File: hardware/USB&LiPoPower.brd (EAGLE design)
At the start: 47 x 40.5 mm, 68 parts, among them IC1 4066D, IC2 4066D, IC3 HT7750A_SOT23-3, IC4 I-02247_NJM2845, T1 IRLML5203, T2 IRLML5203, T3 IRLML5203, T4 IRLML5203

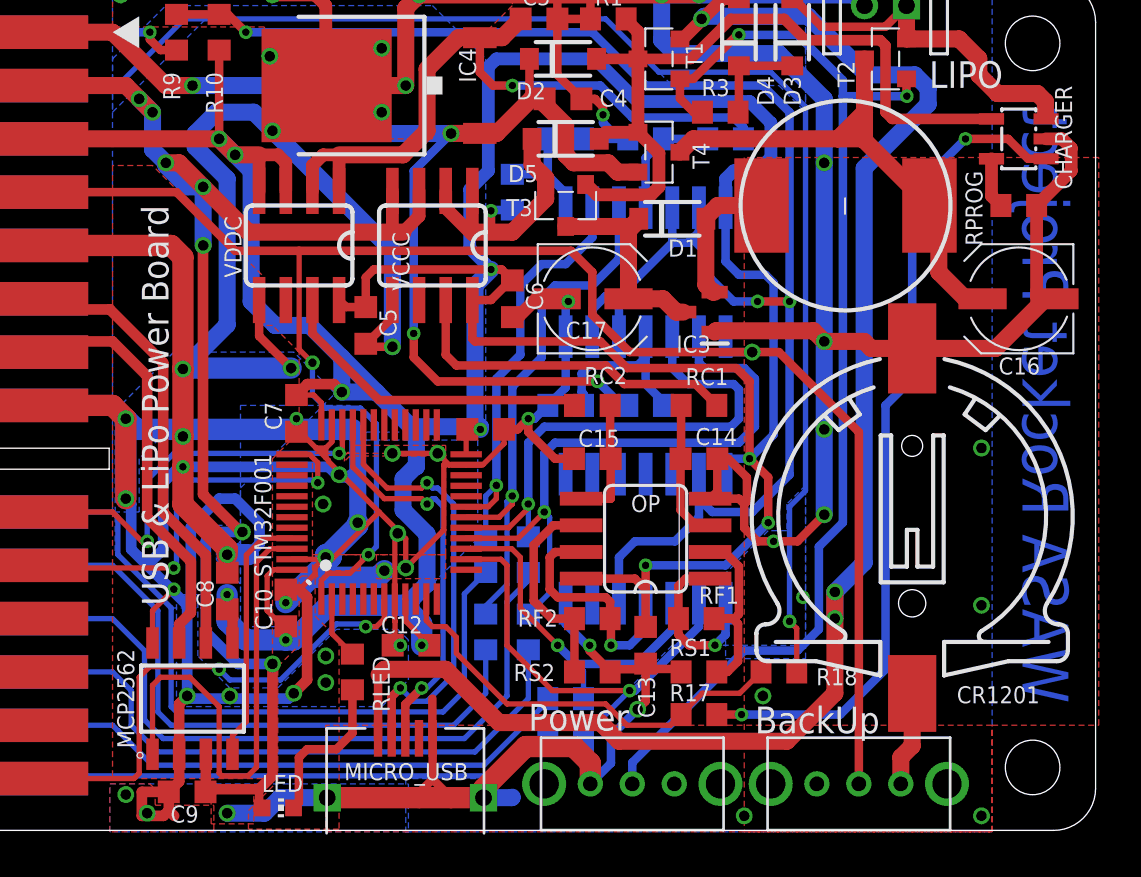
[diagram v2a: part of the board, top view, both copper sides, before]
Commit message: Clean silk print
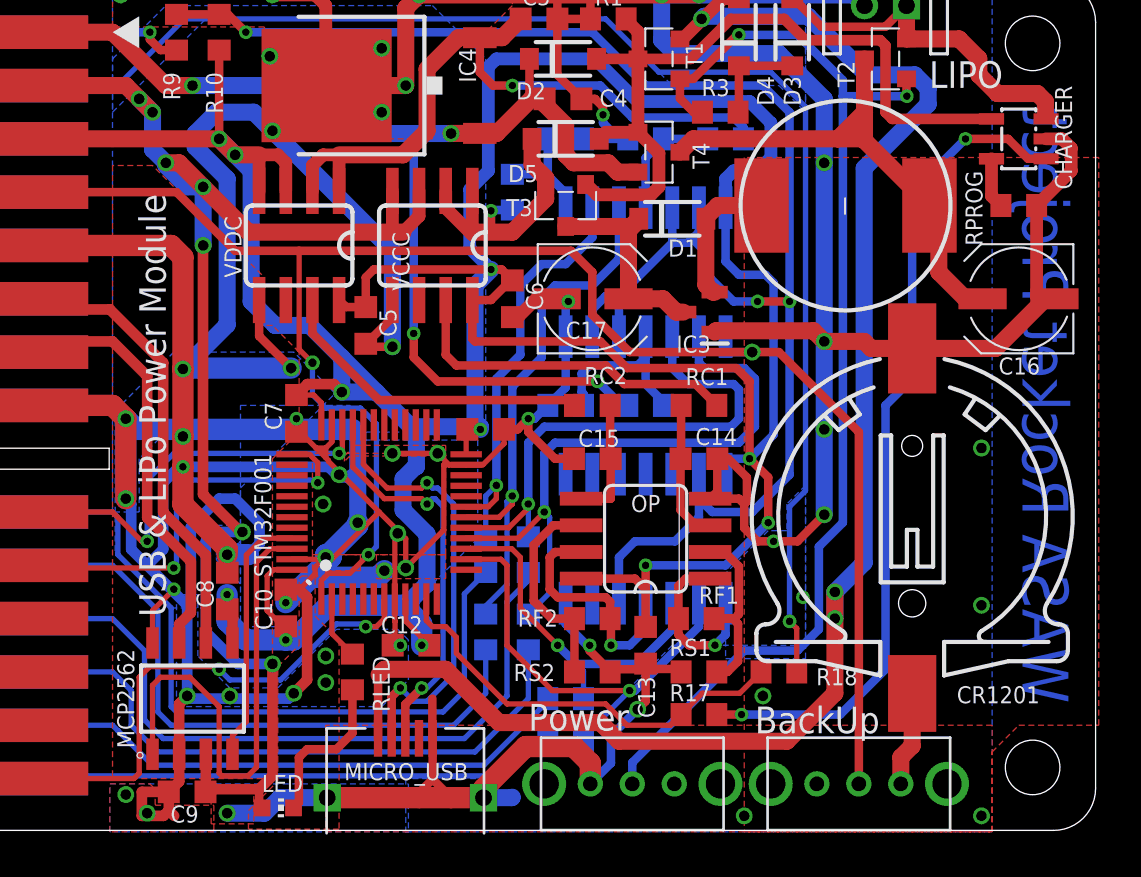
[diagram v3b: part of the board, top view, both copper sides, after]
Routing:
- net VPP: track 59.8 -> 60.7 mm
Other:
- board text added: "Designed by @fujiy0, 2019"
- board text added: "USB & LiPo Power Module"
- board text removed: "USB & LiPo Power Board"
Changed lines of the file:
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@@
 <layer number="14" name="Route14" color="22" fill="1" visible="no" active="no"/>
 <layer number="15" name="Route15" color="23" fill="1" visible="no" active="no"/>
-<layer number="16" name="Bottom" color="1" fill="1" visible="no" active="yes"/>
+<layer number="16" name="Bottom" color="1" fill="1" visible="yes" active="yes"/>
 <layer number="17" name="Pads" color="2" fill="1" visible="yes" active="yes"/>
 <layer number="18" name="Vias" color="2" fill="1" visible="yes" active="yes"/>
@@
 <layer number="20" name="Dimension" color="24" fill="1" visible="yes" active="yes"/>
 <layer number="21" name="tPlace" color="7" fill="1" visible="yes" active="yes"/>
-<layer number="22" name="bPlace" color="7" fill="1" visible="no" active="yes"/>
+<layer number="22" name="bPlace" color="7" fill="1" visible="yes" active="yes"/>
 <layer number="23" name="tOrigins" color="15" fill="1" visible="yes" active="yes"/>
-<layer number="24" name="bOrigins" color="15" fill="1" visible="no" active="yes"/>
+<layer number="24" name="bOrigins" color="15" fill="1" visible="yes" active="yes"/>
 <layer number="25" name="tNames" color="7" fill="1" visible="yes" active="yes"/>
-<layer number="26" name="bNames" color="7" fill="1" visible="no" active="yes"/>
+<layer number="26" name="bNames" color="7" fill="1" visible="yes" active="yes"/>
 <layer number="27" name="tValues" color="7" fill="1" visible="no" active="yes"/>
 <layer number="28" name="bValues" color="7" fill="1" visible="no" active="yes"/>
@@
 <layer number="38" name="bTest" color="7" fill="1" visible="no" active="yes"/>
 <layer number="39" name="tKeepout" color="4" fill="11" visible="yes" active="yes"/>
-<layer number="40" name="bKeepout" color="1" fill="11" visible="no" active="yes"/>
+<layer number="40" name="bKeepout" color="1" fill="11" visible="yes" active="yes"/>
 <layer number="41" name="tRestrict" color="4" fill="10" visible="yes" active="yes"/>
-<layer number="42" name="bRestrict" color="1" fill="10" visible="no" active="yes"/>
+<layer number="42" name="bRestrict" color="1" fill="10" visible="yes" active="yes"/>
 <layer number="43" name="vRestrict" color="2" fill="10" visible="no" active="yes"/>
 <layer number="44" name="Drills" color="7" fill="1" visible="no" active="yes"/>
@@
 <layer number="50" name="dxf" color="7" fill="1" visible="no" active="no"/>
 <layer number="51" name="tDocu" color="7" fill="1" visible="yes" active="yes"/>
-<layer number="52" name="bDocu" color="7" fill="1" visible="no" active="yes"/>
+<layer number="52" name="bDocu" color="7" fill="1" visible="yes" active="yes"/>
 <layer number="53" name="tGND_GNDA" color="7" fill="9" visible="no" active="no"/>
 <layer number="54" name="bGND_GNDA" color="1" fill="9" visible="no" active="no"/>
@@
 <vertex x="11.43" y="17.018"/>
 </polygon>
-<text x="12.192" y="0" size="1.27" layer="25" font="vector" rot="R90" align="center">USB &amp; LiPo Power Board</text>
+<text x="12.065" y="0" size="1.27" layer="25" font="vector" rot="R90" align="center">USB &amp; LiPo Power Module</text>
+<text x="50.8" y="-9.017" size="0.8128" layer="30" font="vector" rot="MR270" align="center">Designed by @fujiy0, 2019</text>
 </plain>
 <attributes>
@@
 <vertex x="40.259" y="-20.32"/>
 <vertex x="52.07" y="-20.32"/>
-<vertex x="52.07" y="-15.24"/>
+<vertex x="52.07" y="-16.51"/>
+<vertex x="53.34" y="-15.24"/>
 </polygon>
 <via x="44.069" y="11.557" extent="1-16" drill="0.5"/>
@@
 <wire x1="24.511" y1="2.286" x2="24.511" y2="3.429" width="0.4064" layer="1"/>
 <via x="24.511" y="3.429" extent="1-16" drill="0.35"/>
-<wire x1="24.511" y1="3.429" x2="24.511" y2="11.176" width="0.4064" layer="16"/>
+<wire x1="24.511" y1="3.429" x2="24.511" y2="12.7" width="0.4064" layer="16"/>
 <wire x1="27.66" y1="12.96" x2="26.295" y2="12.96" width="0.8128" layer="1"/>
 <wire x1="26.295" y1="12.96" x2="26.289" y2="12.954" width="0.8128" layer="1"/>
 <via x="26.289" y="12.954" extent="1-16" drill="0.5"/>
-<wire x1="24.511" y1="11.176" x2="26.289" y2="12.954" width="0.4064" layer="16"/>
+<wire x1="24.765" y1="12.954" x2="26.289" y2="12.954" width="0.4064" layer="16"/>
+<wire x1="24.765" y1="12.954" x2="24.511" y2="12.7" width="0.4064" layer="16"/>
 <wire x1="26.289" y1="12.954" x2="22.606" y2="12.954" width="0.8128" layer="16"/>
 <wire x1="22.606" y1="12.954" x2="20.32" y2="15.24" width="0.8128" layer="16"/>

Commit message: Some fixes
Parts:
- RPROG: value (none) -> 4.7k
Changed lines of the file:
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@@
 <layer number="14" name="Route14" color="22" fill="1" visible="no" active="no"/>
 <layer number="15" name="Route15" color="23" fill="1" visible="no" active="no"/>
-<layer number="16" name="Bottom" color="1" fill="1" visible="yes" active="yes"/>
+<layer number="16" name="Bottom" color="1" fill="1" visible="no" active="yes"/>
 <layer number="17" name="Pads" color="2" fill="1" visible="yes" active="yes"/>
 <layer number="18" name="Vias" color="2" fill="1" visible="yes" active="yes"/>
@@
 <layer number="20" name="Dimension" color="24" fill="1" visible="yes" active="yes"/>
 <layer number="21" name="tPlace" color="7" fill="1" visible="yes" active="yes"/>
-<layer number="22" name="bPlace" color="7" fill="1" visible="yes" active="yes"/>
+<layer number="22" name="bPlace" color="7" fill="1" visible="no" active="yes"/>
 <layer number="23" name="tOrigins" color="15" fill="1" visible="yes" active="yes"/>
-<layer number="24" name="bOrigins" color="15" fill="1" visible="yes" active="yes"/>
+<layer number="24" name="bOrigins" color="15" fill="1" visible="no" active="yes"/>
 <layer number="25" name="tNames" color="7" fill="1" visible="yes" active="yes"/>
-<layer number="26" name="bNames" color="7" fill="1" visible="yes" active="yes"/>
+<layer number="26" name="bNames" color="7" fill="1" visible="no" active="yes"/>
 <layer number="27" name="tValues" color="7" fill="1" visible="no" active="yes"/>
 <layer number="28" name="bValues" color="7" fill="1" visible="no" active="yes"/>
@@
 <layer number="38" name="bTest" color="7" fill="1" visible="no" active="yes"/>
 <layer number="39" name="tKeepout" color="4" fill="11" visible="yes" active="yes"/>
-<layer number="40" name="bKeepout" color="1" fill="11" visible="yes" active="yes"/>
+<layer number="40" name="bKeepout" color="1" fill="11" visible="no" active="yes"/>
 <layer number="41" name="tRestrict" color="4" fill="10" visible="yes" active="yes"/>
-<layer number="42" name="bRestrict" color="1" fill="10" visible="yes" active="yes"/>
+<layer number="42" name="bRestrict" color="1" fill="10" visible="no" active="yes"/>
 <layer number="43" name="vRestrict" color="2" fill="10" visible="no" active="yes"/>
 <layer number="44" name="Drills" color="7" fill="1" visible="no" active="yes"/>
@@
 <layer number="50" name="dxf" color="7" fill="1" visible="no" active="no"/>
 <layer number="51" name="tDocu" color="7" fill="1" visible="yes" active="yes"/>
-<layer number="52" name="bDocu" color="7" fill="1" visible="yes" active="yes"/>
+<layer number="52" name="bDocu" color="7" fill="1" visible="no" active="yes"/>
 <layer number="53" name="tGND_GNDA" color="7" fill="9" visible="no" active="no"/>
 <layer number="54" name="bGND_GNDA" color="1" fill="9" visible="no" active="no"/>
@@
 <attribute name="VALUE" x="30.48" y="1.27" size="1.016" layer="27"/>
 </element>
-<element name="RPROG" library="rcl" library_urn="urn:adsk.eagle:library:334" package="R0603" package3d_urn="urn:adsk.eagle:package:23555/3" value="" x="53.34" y="9.525" smashed="yes" rot="R180">
+<element name="RPROG" library="rcl" library_urn="urn:adsk.eagle:library:334" package="R0603" package3d_urn="urn:adsk.eagle:package:23555/3" value="4.7k" x="53.34" y="9.525" smashed="yes" rot="R180">
 <attribute name="NAME" x="50.8" y="11.176" size="0.8128" layer="25" font="vector" rot="R270"/>
 <attribute name="POPULARITY" value="77" x="53.34" y="9.525" size="1.778" layer="27" rot="R180" display="off"/>
